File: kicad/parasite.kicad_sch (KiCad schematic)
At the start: 42 parts, among them J1 JLINK-6PIN, U1 E73-2G4M08S1C-52840, U2 BQ25504, Y1 32.768kHz

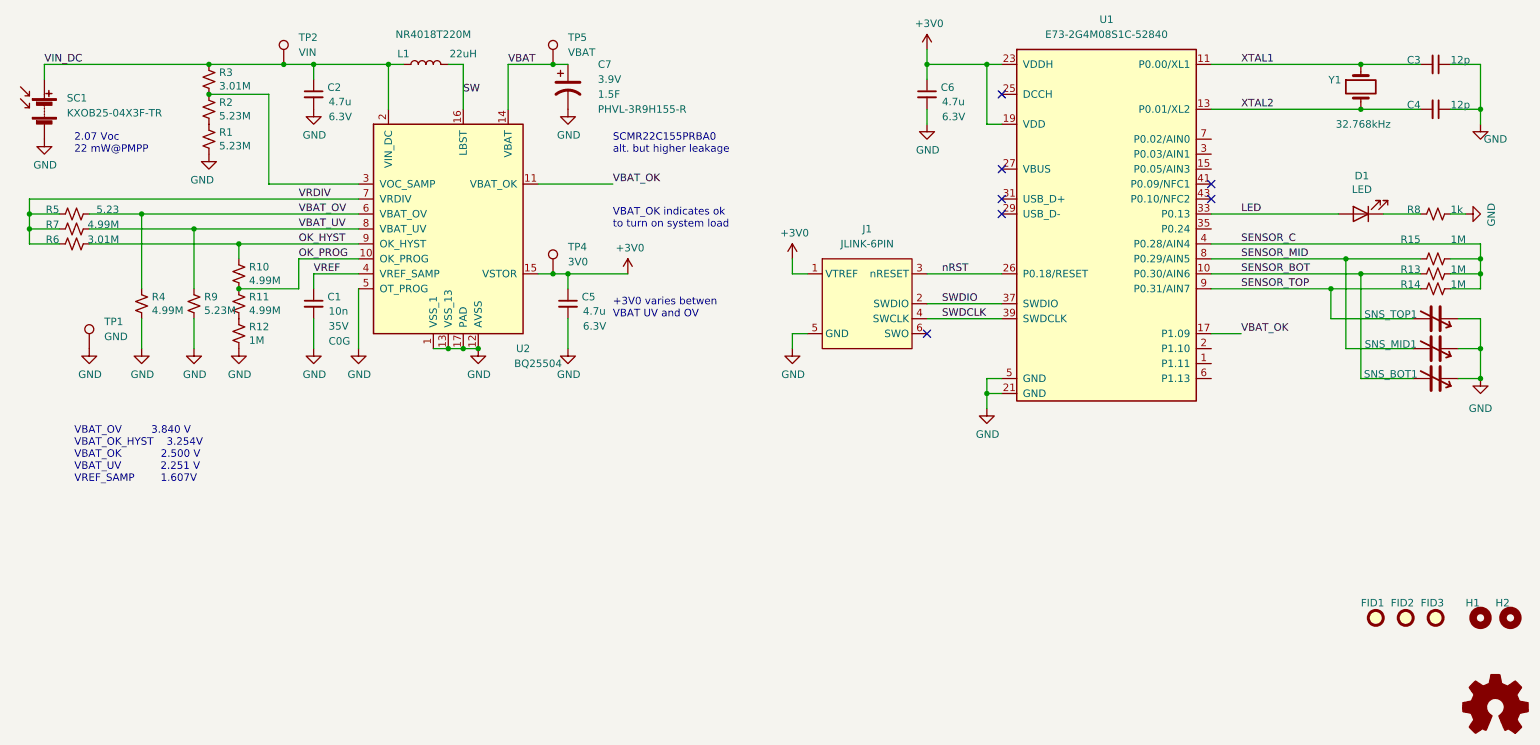
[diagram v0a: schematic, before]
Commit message: Cleared remaining DRC, add JLCPCB part numbers
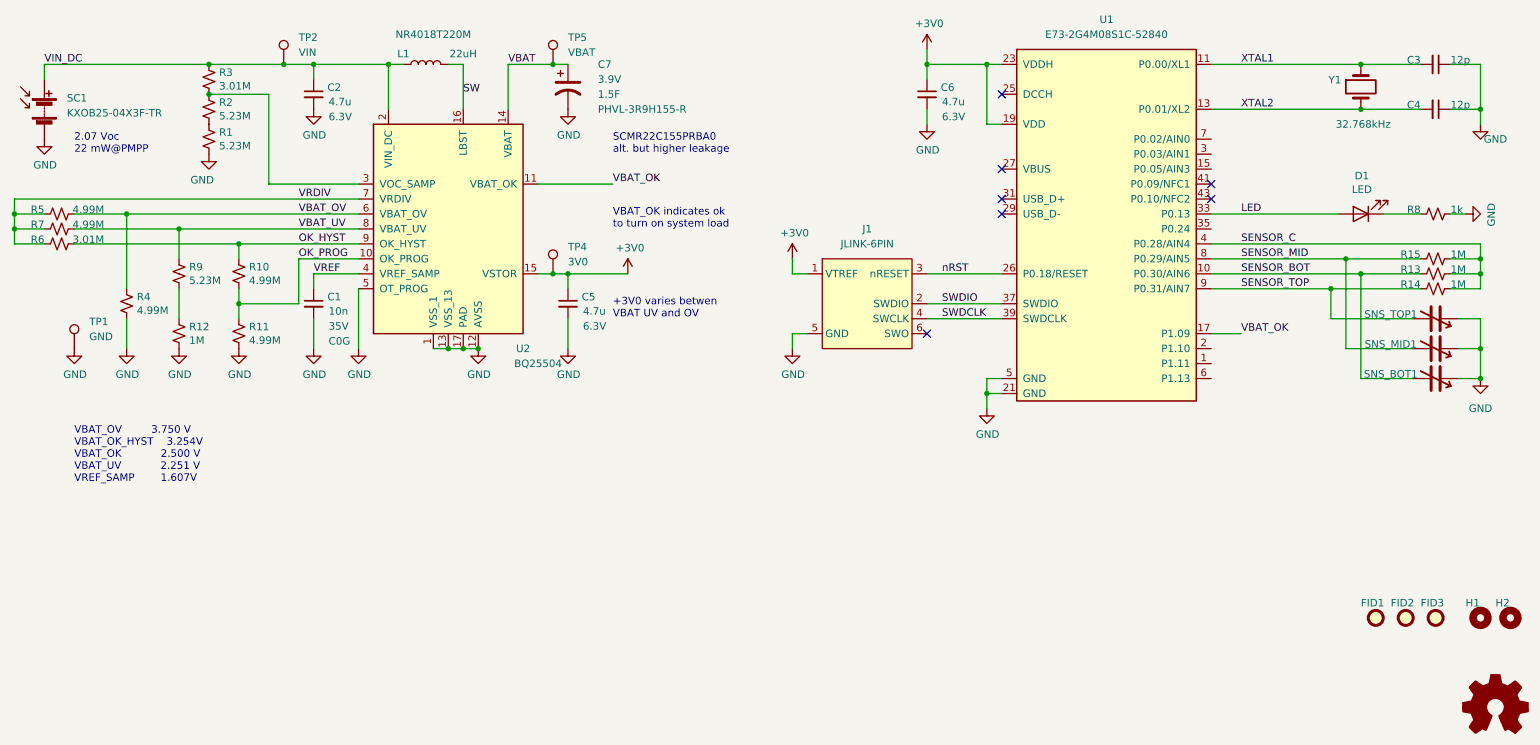
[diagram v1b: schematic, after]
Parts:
- C2, C5, C6: LCSC C1525 -> C23733
- D1: LCSC C2286 -> C160479
- R5: value 5.23 -> 4.99M; LCSC C11702 -> C137963
- U1: footprint nrfmicro:E73-2G4M08S1C-52840 -> solar-bug:E73-2G4M08S1C-52840
- Y1: LCSC C179633 -> C398713
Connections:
- net GND: now also R11.2; no longer R9.2
- net at R12.1: now also R9.2; no longer R11.2
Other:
- note added: "VBAT_OV 3.750 V VBAT_OK_HYST 3.254V VBAT_OK 2.500 V VBAT_UV 2.251 V VREF_SAMP 1.607V"
- note removed: "VBAT_OV 3.840 V VBAT_OK_HYST 3.254V VBAT_OK 2.500 V VBAT_UV 2.251 V VREF_SAMP 1.607V"
- moved on the sheet: R11, R12, R4, R6, R7, R9, TP1
